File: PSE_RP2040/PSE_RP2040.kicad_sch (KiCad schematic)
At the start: 68 parts, among them J1 USB_B, J2 USB_B_Micro, J4 Conn_01x03, SW1 SW_Push, SW2 SW_Push, U1 RP2040, U2 PCF8563T, U5 W25Q16JVUXIQ //ss, U6 PAM7Q, Y1 Crystal_GND3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

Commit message: modifiche lezione
usb mini,
check s1b
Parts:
- removed J2: USB_B_Micro, Connector_USB:USB_Micro-B_Wuerth_629105150521, symbol Connector:USB_B_Micro
- added J2: (no value), symbol Connector:USB_B_Mini
- C1: value (none) -> 0.1F; footprint (none) -> Capacitor_THT:CP_Radial_D10.0mm_P5.00mm
- D1: footprint (none) -> Diode_SMD:D_SMA
- D2: value D_Bridge_+-AA -> (none); footprint Package_SO:SO-4_4.4x3.6mm_P2.54mm -> (none)
- D3: value D_Bridge_+-AA -> (none)
- IC2: value (none) -> SAM-M8Q-0; footprint (none) -> PSE2021:SAM-M8Q
- J1: value USB_B -> (none); footprint Connector_USB:USB_B_OST_USB-B1HSxx_Horizontal -> (none)
- J3: value (none) -> 8P8C_LED; footprint (none) -> PSE2021:RJ45_Amphenol_RJHSE-5081
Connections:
- net GND: now also J2.5 (GND), J2.6 (Shield)
- net USB_DN: now also J2.2 (D-)
- net USB_DP: now also J2.3 (D+)
- net VUSB: now also J2.1 (VBUS)
- net GPIO22 renamed GPIO22_R
- net GPIO23 renamed GPIO23_G
- net GPIO24 renamed GPIO24_B
- net GPS_RESET: no longer names the net of IC2.18 (RESET_N)
- no-connect marks 13 -> 14
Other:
- note added: "Localizzazione: scheda spezzabile?"
- note removed: "Localizzazione"
- moved on the sheet: C1, C12, C13, C14, C7, D1, D4, IC2, J4, Q2, R2, R27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

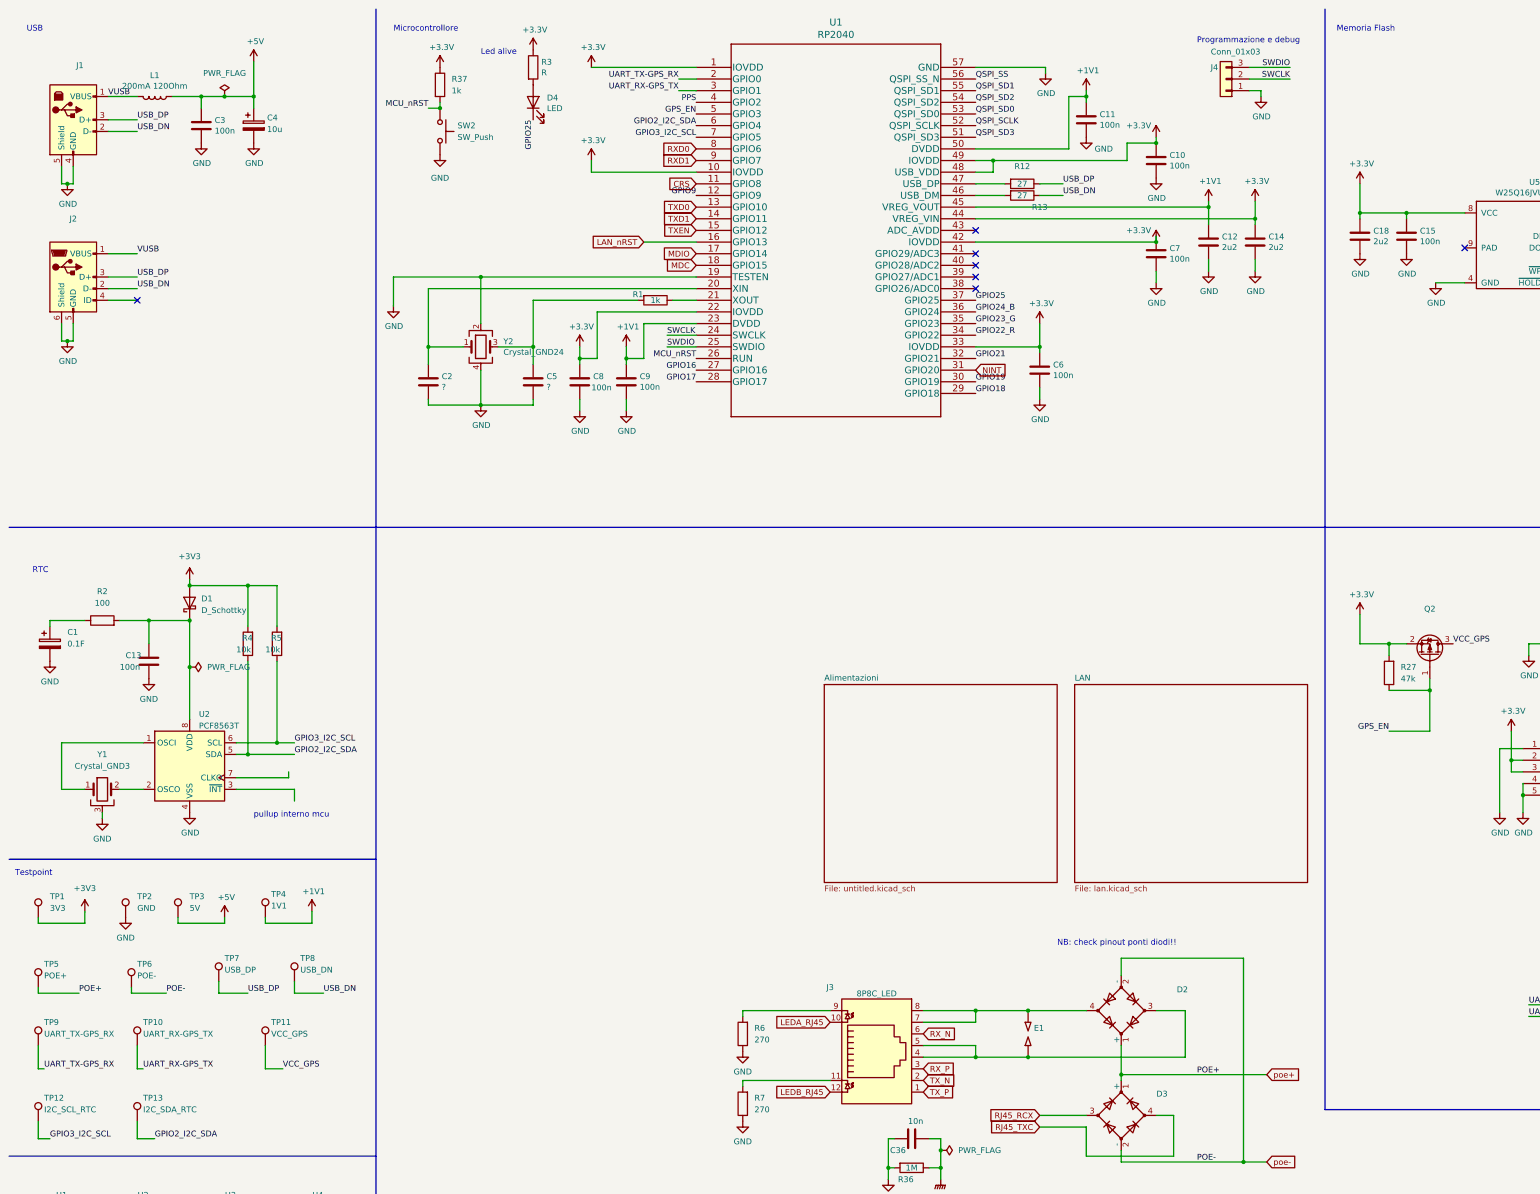
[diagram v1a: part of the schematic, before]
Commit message: footprint
cambiato footprint rp2040 (ora c'è quello con le vias) e footprint tps2375
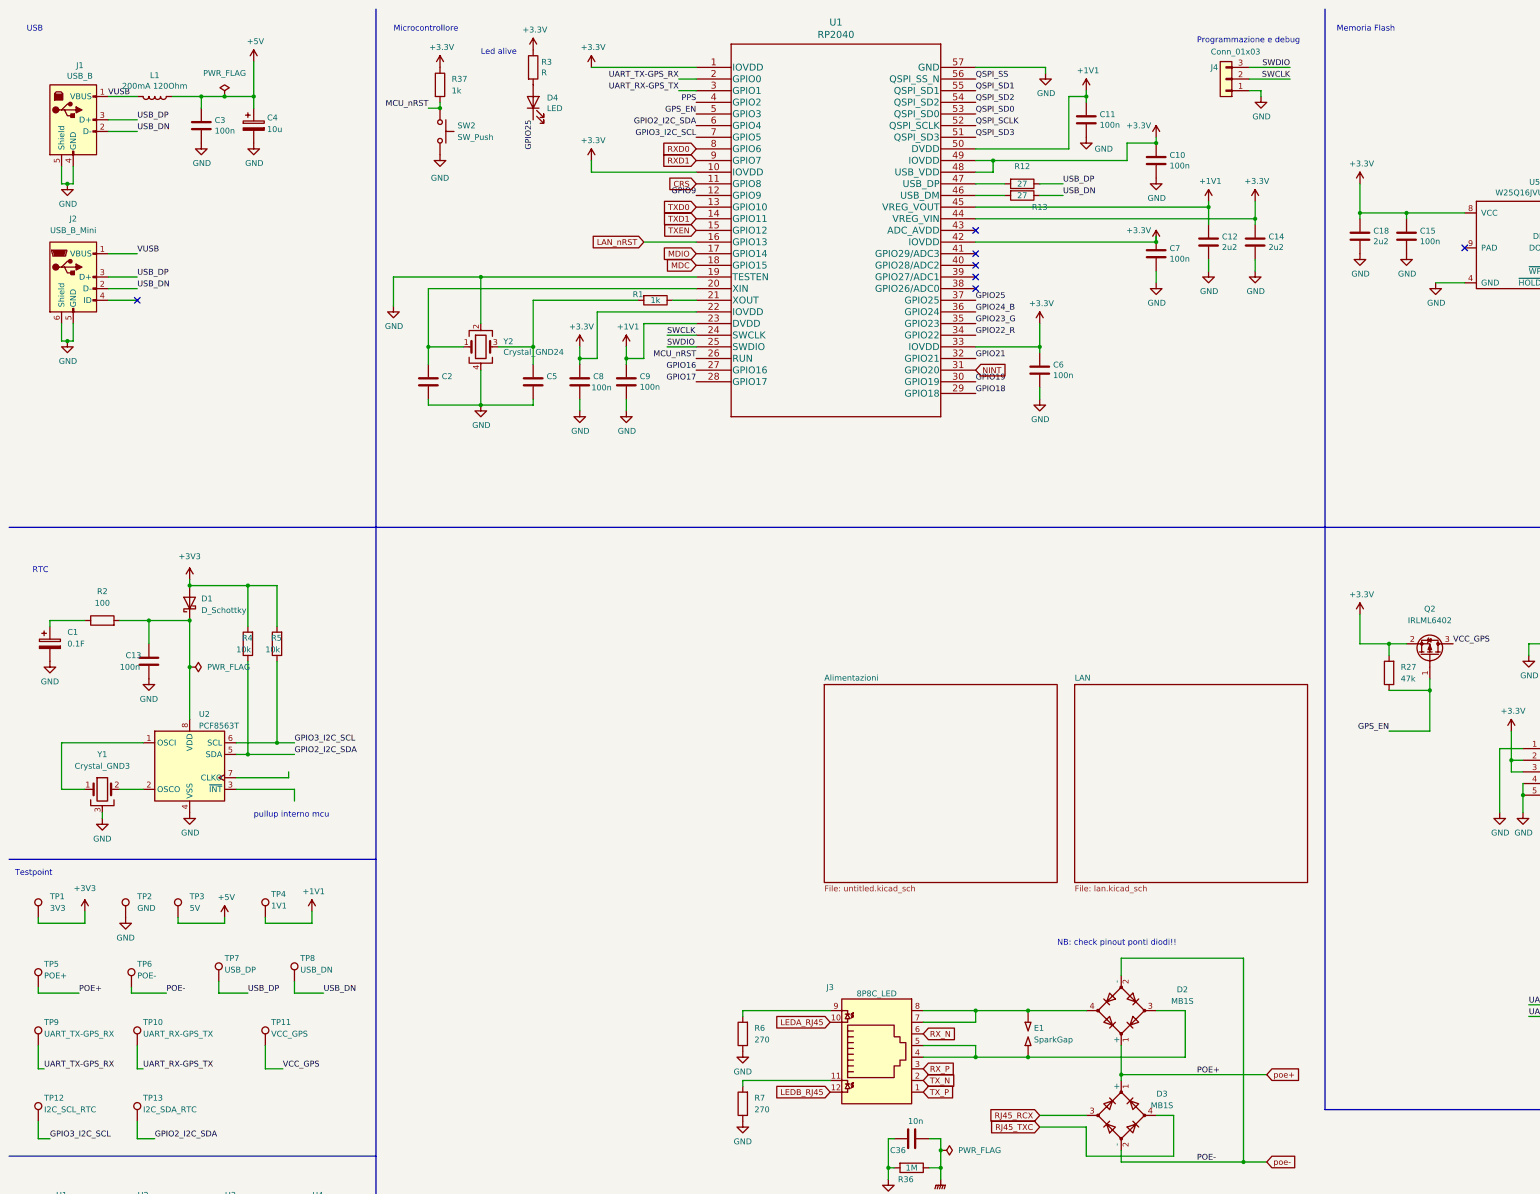
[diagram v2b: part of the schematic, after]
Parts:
- C2: value ? -> (none); footprint Capacitor_SMD:C_0603_1608Metric -> (none)
- C5: value ? -> (none)
- D2: value (none) -> MB1S; footprint (none) -> Package_SO:SO-4_4.4x3.6mm_P2.54mm
- D3: value (none) -> MB1S
- E1: value (none) -> SparkGap; footprint (none) -> PSE2021:SPARK_GAP_TRIANGLE
- J1: value (none) -> USB_B; footprint (none) -> Connector_USB:USB_B_OST_USB-B1HSxx_Horizontal
- J2: value (none) -> USB_B_Mini; footprint (none) -> Connector_USB:USB_Mini-B_Wuerth_65100516121_Horizontal
- Q2: value (none) -> IRLML6402; footprint (none) -> Package_TO_SOT_SMD:SOT-23
- U1: footprint RP2040:RP2040 -> (none)
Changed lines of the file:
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@@
       (effects (font (size 1.524 1.524)))
     )
-    (property "Footprint" "RP2040:RP2040" (id 2) (at 193.04 19.304 0)
+    (property "Footprint" "" (id 2) (at 193.04 19.304 0)
       (effects (font (size 1.524 1.524)) hide)
     )
@@
     (in_bom yes) (on_board yes)
     (property "Reference" "J1" (id 0) (at 28.1178 24.9682 0))
-    (property "Value" "" (id 1) (at 28.1178 27.2796 0))
-    (property "Footprint" "" (id 2) (at 30.48 38.1 0)
+    (property "Value" "USB_B" (id 1) (at 28.1178 27.2796 0))
+    (property "Footprint" "Connector_USB:USB_B_OST_USB-B1HSxx_Horizontal" (id 2) (at 30.48 38.1 0)
       (effects (font (size 1.27 1.27)) hide)
     )
@@
       (effects (font (size 1.27 1.27)) (justify left))
     )
-    (property "Value" "?" (id 1) (at 107.061 95.123 0)
-      (effects (font (size 1.27 1.27)) (justify left))
-    )
-    (property "Footprint" "Capacitor_SMD:C_0603_1608Metric" (id 2) (at 105.1052 97.79 0)
+    (property "Value" "" (id 1) (at 107.061 95.123 0)
+      (effects (font (size 1.27 1.27)) (justify left))
+    )
+    (property "Footprint" "" (id 2) (at 105.1052 97.79 0)
       (effects (font (size 1.27 1.27)) hide)
     )
@@
       (effects (font (size 1.27 1.27)) (justify left))
     )
-    (property "Value" "?" (id 1) (at 129.921 95.123 0)
+    (property "Value" "" (id 1) (at 129.921 95.123 0)
       (effects (font (size 1.27 1.27)) (justify left))
     )
@@
     (in_bom yes) (on_board yes) (fields_autoplaced)
     (property "Reference" "Q2" (id 0) (at 322.58 143.51 90))
-    (property "Value" "" (id 1) (at 322.58 146.05 90))
-    (property "Footprint" "" (id 2) (at 325.12 148.59 0)
+    (property "Value" "IRLML6402" (id 1) (at 322.58 146.05 90))
+    (property "Footprint" "Package_TO_SOT_SMD:SOT-23" (id 2) (at 325.12 148.59 0)
       (effects (font (size 1.27 1.27)) hide)
     )
@@
       (effects (font (size 1.27 1.27)) (justify right))
     )
-    (property "Value" "" (id 1) (at 236.22 237.4899 90)
+    (property "Value" "SparkGap" (id 1) (at 236.22 237.4899 90)
       (effects (font (size 1.27 1.27)) (justify right))
     )
-    (property "Footprint" "" (id 2) (at 236.728 236.22 0)
+    (property "Footprint" "PSE2021:SPARK_GAP_TRIANGLE" (id 2) (at 236.728 236.22 0)
       (effects (font (size 1.27 1.27)) hide)
     )
@@
     (in_bom yes) (on_board yes) (fields_autoplaced)
     (property "Reference" "D3" (id 0) (at 264.16 249.301 90))
-    (property "Value" "" (id 1) (at 264.16 251.841 90))
+    (property "Value" "MB1S" (id 1) (at 264.16 251.841 90))
     (property "Footprint" "Package_SO:SO-4_4.4x3.6mm_P2.54mm" (id 2) (at 255.27 254 0)
       (effects (font (size 1.27 1.27)) hide)
@@
     (in_bom yes) (on_board yes) (fields_autoplaced)
     (property "Reference" "D2" (id 0) (at 268.6058 226.5511 90))
-    (property "Value" "" (id 1) (at 268.6058 229.088 90))
-    (property "Footprint" "" (id 2) (at 255.27 231.14 0)
+    (property "Value" "MB1S" (id 1) (at 268.6058 229.088 90))
+    (property "Footprint" "Package_SO:SO-4_4.4x3.6mm_P2.54mm" (id 2) (at 255.27 231.14 0)
       (effects (font (size 1.27 1.27)) hide)
     )
@@
     (in_bom yes) (on_board yes) (fields_autoplaced)
     (property "Reference" "J2" (id 0) (at 26.67 58.42 0))
-    (property "Value" "" (id 1) (at 26.67 60.96 0))
-    (property "Footprint" "" (id 2) (at 30.48 72.39 0)
+    (property "Value" "USB_B_Mini" (id 1) (at 26.67 60.96 0))
+    (property "Footprint" "Connector_USB:USB_Mini-B_Wuerth_65100516121_Horizontal" (id 2) (at 30.48 72.39 0)
       (effects (font (size 1.27 1.27)) hide)
     )
@@
     )
     (path "/00000000-0000-0000-0000-0000622ecf54"
-      (reference "C2") (unit 1) (value "?") (footprint "Capacitor_SMD:C_0603_1608Metric")
+      (reference "C2") (unit 1) (value "12p") (footprint "Capacitor_SMD:C_0603_1608Metric")
     )
     (path "/00000000-0000-0000-0000-0000622e3945"
@@
     )
     (path "/00000000-0000-0000-0000-0000622eddb4"
-      (reference "C5") (unit 1) (value "?") (footprint "Capacitor_SMD:C_0603_1608Metric")
+      (reference "C5") (unit 1) (value "12p") (footprint "Capacitor_SMD:C_0603_1608Metric")
     )
     (path "/00000000-0000-0000-0000-0000627c14d9"
@@
     )
     (path "/00000000-0000-0000-0000-0000622dcbd6"
-      (reference "U1") (unit 1) (value "RP2040") (footprint "RP2040:RP2040")
+      (reference "U1") (unit 1) (value "RP2040") (footprint "PSE2021:RP2040-QFN-56")
     )
     (path "/52aa4775-b499-4300-a415-65cd614bc4ca"
@@
     )
     (path "/cfa038c0-a49f-45bf-b6e3-72692695ea2c/68a6667b-00d5-464a-a99c-4f218dc7c7d1"
-      (reference "U7") (unit 1) (value "TPS2375-1") (footprint "Package_SO:TSSOP-8_4.4x3mm_P0.65mm")
+      (reference "U7") (unit 1) (value "TPS2375-1") (footprint "Package_SO:SOIC-8_5.275x5.275mm_P1.27mm")
     )
     (path "/cfa038c0-a49f-45bf-b6e3-72692695ea2c/2592c0ef-fef1-4f88-b620-5257f7b41b2f"

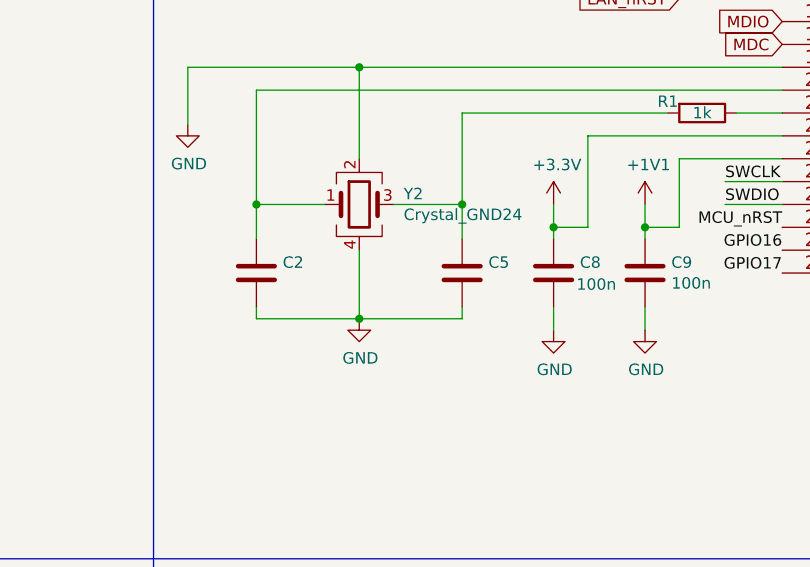
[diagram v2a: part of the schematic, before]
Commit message: allungate pad footprint micro
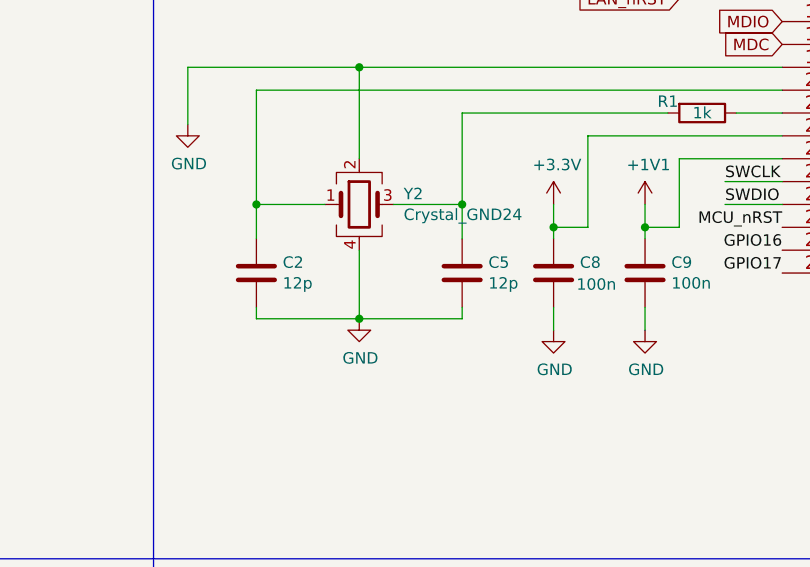
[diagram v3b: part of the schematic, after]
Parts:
- C2: value (none) -> 12p; footprint (none) -> Capacitor_SMD:C_0603_1608Metric
- C5: value (none) -> 12p
- U1: footprint (none) -> PSE2021:RP2040-QFN-56
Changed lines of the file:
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@@
       (effects (font (size 1.524 1.524)))
     )
-    (property "Footprint" "" (id 2) (at 193.04 19.304 0)
+    (property "Footprint" "PSE2021:RP2040-QFN-56" (id 2) (at 193.04 19.304 0)
       (effects (font (size 1.524 1.524)) hide)
     )
@@
       (effects (font (size 1.27 1.27)) (justify left))
     )
-    (property "Value" "" (id 1) (at 107.061 95.123 0)
-      (effects (font (size 1.27 1.27)) (justify left))
-    )
-    (property "Footprint" "" (id 2) (at 105.1052 97.79 0)
+    (property "Value" "12p" (id 1) (at 107.061 95.123 0)
+      (effects (font (size 1.27 1.27)) (justify left))
+    )
+    (property "Footprint" "Capacitor_SMD:C_0603_1608Metric" (id 2) (at 105.1052 97.79 0)
       (effects (font (size 1.27 1.27)) hide)
     )
@@
       (effects (font (size 1.27 1.27)) (justify left))
     )
-    (property "Value" "" (id 1) (at 129.921 95.123 0)
-      (effects (font (size 1.27 1.27)) (justify left))
-    )
+    (property "Value" "12p" (id 1) (at 129.921 95.123 0)
+      (effects (font (size 1.27 1.27)) (justify left))
+    )
